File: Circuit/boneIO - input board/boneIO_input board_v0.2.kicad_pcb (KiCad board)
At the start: 2 copper layers, 256 x 74 mm, 213 parts, among them J1 Screw_Terminal_01x08, J10 BeagleBone_Black_Header, J11 BeagleBone_Black_Header, J12 Conn_02x04_Odd_Even, J13 Screw_Terminal_01x04, J2 Screw_Terminal_01x08, J3 Screw_Terminal_01x08, J4 Screw_Terminal_01x08, J5 Screw_Terminal_01x08, J6 Screw_Terminal_01x08, J7 Screw_Terminal_01x08, J8 Screw_Terminal_01x08, J9 Screw_Terminal_01x08, SW1 SW_Push, U1 EL357N-G, U10 EL357N-G, U11 EL357N-G, U12 EL357N-G, U13 EL357N-G, U14 EL357N-G, U15 EL357N-G, U16 EL357N-G, U17 EL357N-G, U18 EL357N-G, U19 EL357N-G, U2 EL357N-G, U20 EL357N-G, U21 EL357N-G, U22 EL357N-G, U23 EL357N-G, U24 EL357N-G, U25 EL357N-G, U26 EL357N-G, U27 EL357N-G, U28 RS485, U29 EL357N-G, U3 EL357N-G, U30 EL357N-G, U31 EL357N-G, U32 EL357N-G, U33 DS1307Z+, U34 EL357N-G, U35 EL357N-G, U36 EL357N-G, U37 EL357N-G, U38 EL357N-G, U39 EL357N-G, U4 EL357N-G, U40 EL357N-G, U41 EL357N-G, U42 EL357N-G, U43 EL357N-G, U44 EL357N-G, U45 EL357N-G, U46 P82B96, U47 EL357N-G, U48 EL357N-G, U49 EL357N-G, U5 EL357N-G, U50 EL357N-G, U51 EL357N-G, U52 EL357N-G, U53 EL357N-G, U54 EL357N-G, U55 EL357N-G, U56 EL357N-G, U6 EL357N-G, U7 EL357N-G, U8 EL357N-G, U9 LM2596S-ADJ, Y1 32,788 MHz

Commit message: Revert "Zmiana Nazwy płytki"
This reverts commit 4cfb8962ad837d49dd7d8c96a90ff7a4eda2ea33.
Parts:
- moved U15 126.9 mm to (75.2, 22.1), turned to 0 degrees
- moved U52 116.5 mm to (118.3, -6.89), turned to 0 degrees
- moved U53 98.5 mm to (75.2, 27.7), turned to 0 degrees
- moved U49 91.8 mm to (95.4, 13.0), turned to 0 degrees
- moved U51 90.8 mm to (75.2, 33.4), turned to 0 degrees
- moved U16 90.8 mm to (118.3, -1.25)
- moved U44 66.4 mm to (85.1, 33.1)
- moved R24 63.3 mm to (46.1, 66.0)
- moved R25 63.3 mm to (41.4, 66.0)
- moved C25 63.3 mm to (46.1, 68.7)
- moved C26 63.3 mm to (41.4, 68.7)
- moved U23 63.3 mm to (41.5, 74.2)
- moved U22 63.3 mm to (46.2, 74.2)
- moved U10 59.2 mm to (68.4, 39.0), turned to 0 degrees
- moved U21 36.8 mm to (78.3, 39.0), turned to 0 degrees
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
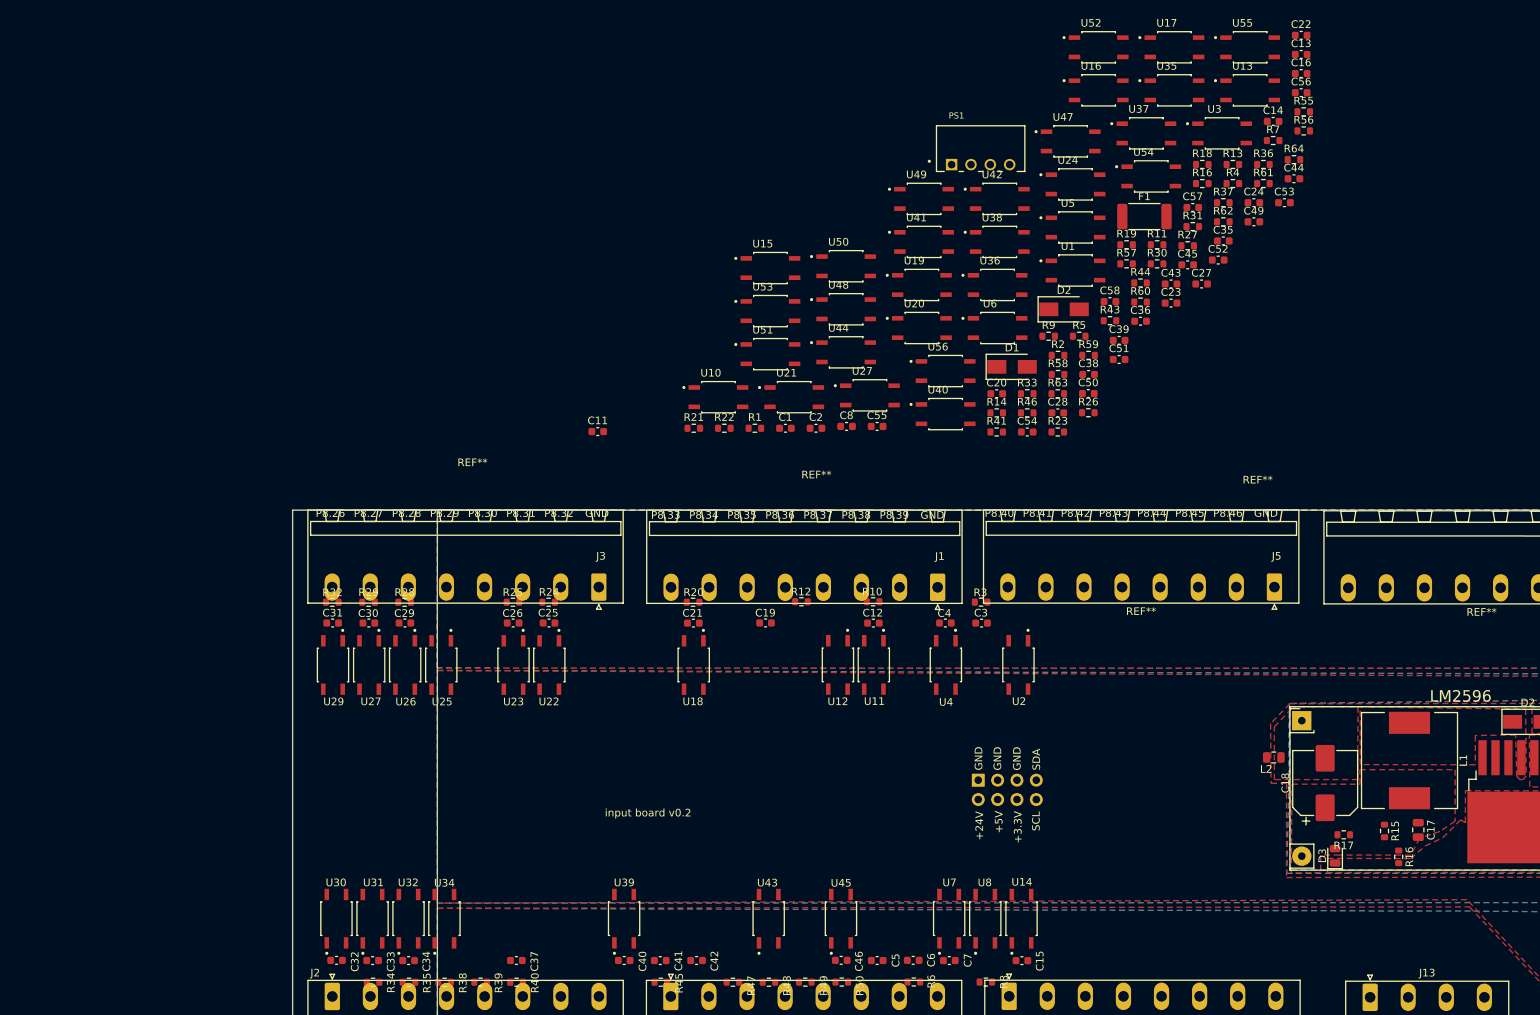
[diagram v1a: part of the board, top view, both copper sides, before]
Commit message: Zmiana Nazwy płytki
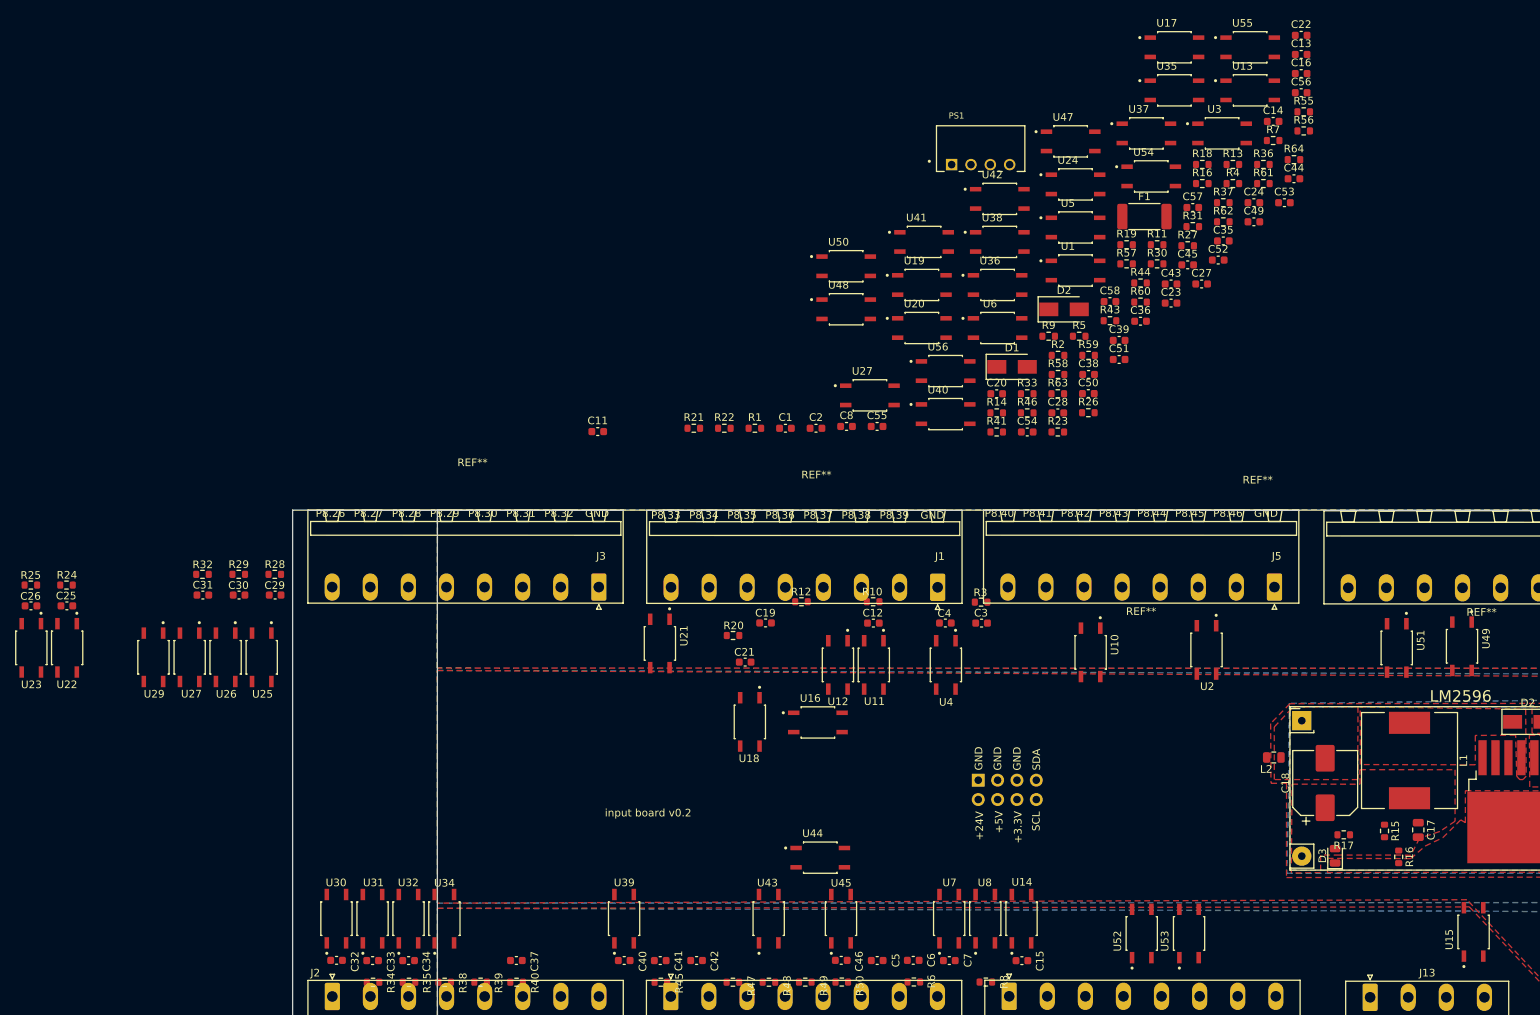
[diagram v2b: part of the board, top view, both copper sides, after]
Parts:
- moved U15 126.9 mm to (167.5, 109.2), turned to 90 degrees
- moved U52 116.5 mm to (123.9, 109.4), turned to 90 degrees
- moved U53 98.5 mm to (130.1, 109.4), turned to 90 degrees
- moved U49 91.8 mm to (166.0, 71.7), turned to 270 degrees
- moved U51 90.8 mm to (157.4, 72.0), turned to 270 degrees
- moved U16 90.8 mm to (81.4, 81.7)
- moved U44 66.4 mm to (81.7, 99.5)
- moved R24 63.3 mm to (-17.2, 63.7)
- moved R25 63.3 mm to (-21.9, 63.7)
- moved C25 63.3 mm to (-17.2, 66.4)
- moved C26 63.3 mm to (-21.9, 66.4)
- moved U23 63.3 mm to (-21.8, 71.9)
- moved U22 63.3 mm to (-17.1, 71.9)
- moved U10 59.2 mm to (117.2, 72.5), turned to 270 degrees
- moved U21 36.8 mm to (60.7, 71.4), turned to 270 degrees
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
